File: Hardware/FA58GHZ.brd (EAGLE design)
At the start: 81.3 x 34.3 mm, 16 parts, among them U1 ATMEGA328P_TQFP, Y1 16MHZ

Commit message: Backup: Working in the Schematic, Footprints and PCB
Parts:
- added C10, C8, C9: 0.1uF, resistor:C0603
- added IC1: MAX4311EEE, maxim:QSOP16
- added JP3: (no value), SparkFun-Connectors:1X06
- added JP4: (no value), SparkFun-Connectors:1X04
- added R10, R11, R12: 1k, resistor:R0603
- added R5, R6, R7: 10k, resistor:R0603
- added R8: 470, resistor:R0603
- added R9: 5k1, resistor:R0603
- added SG1: BUZZERSMD, SparkFun-Electromechanical:BUZZER-CMT1603
- added U2: RX5808, FreakyAttic-EagleLibrary:RX5808
- added X1: SMA, con-coax:J502-ND-142-0701-881/886
- JP1: device SparkFun-Connectors:1X03 -> SparkFun-Connectors:1X03-1MM-RA
- R3, R4: value 10k -> ?
- moved U1 49.5 mm to (10.2, 58.4)
- moved JP1 3.17 mm to (20.3, 8.26)
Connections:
- net N$6 renamed LED
- new net BUT1: U1.32
- new net BUT2: U1.1
- new net CH1: R7.1, U1.14
- new net CH2: R5.1, U1.15
- new net CH3: R6.1, U1.16
- new net N$10: R12.1, U1.9
- new net N$11: SG1.P$2, U1.10
- new net N$12: R12.2, SG1.P$1
- new net N$13: R6.2, U2.P$9
- new net N$14: R5.2, U2.P$8
- new net N$15: R7.2, U2.P$7
- new net N$16: U2.P$11, X1.1
- new net N$6: R8.1, U1.11
- new net N$7: R9.1, U1.13
- new net N$8: R10.1, U1.30
- new net N$9: R11.1, U1.31
- new net OSD: IC1.5, R8.2, R9.2
- new net RSSI1: JP4.2, U1.19, U2.P$4
- new net RSSI2: JP4.4, U1.22
- new net SEL0: IC1.2
- new net SEL1: IC1.1
- new net VIDEO1: IC1.7, JP3.2, U2.P$2
- new net VIDEO2: IC1.10, JP3.4
- new net VIDEO3: IC1.12, JP3.6
- new net VIDEO_OUT: IC1.15, IC1.16
- net AN_VPOW: now also C9.2
- net GND: now also C10.1, C8.2, C9.1, IC1.13, JP3.1, JP3.3, JP3.5, JP4.1, JP4.3, U2.P$1, U2.P$10, U2.P$12, U2.P$6, X1.G@1, X1.G@2, X1.G@3, X1.G@4
- net VCC: now also C10.2, C8.1, IC1.14, IC1.4, U2.P$5
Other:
- board size 81.3 x 34.3 mm -> 108 x 78.7 mm

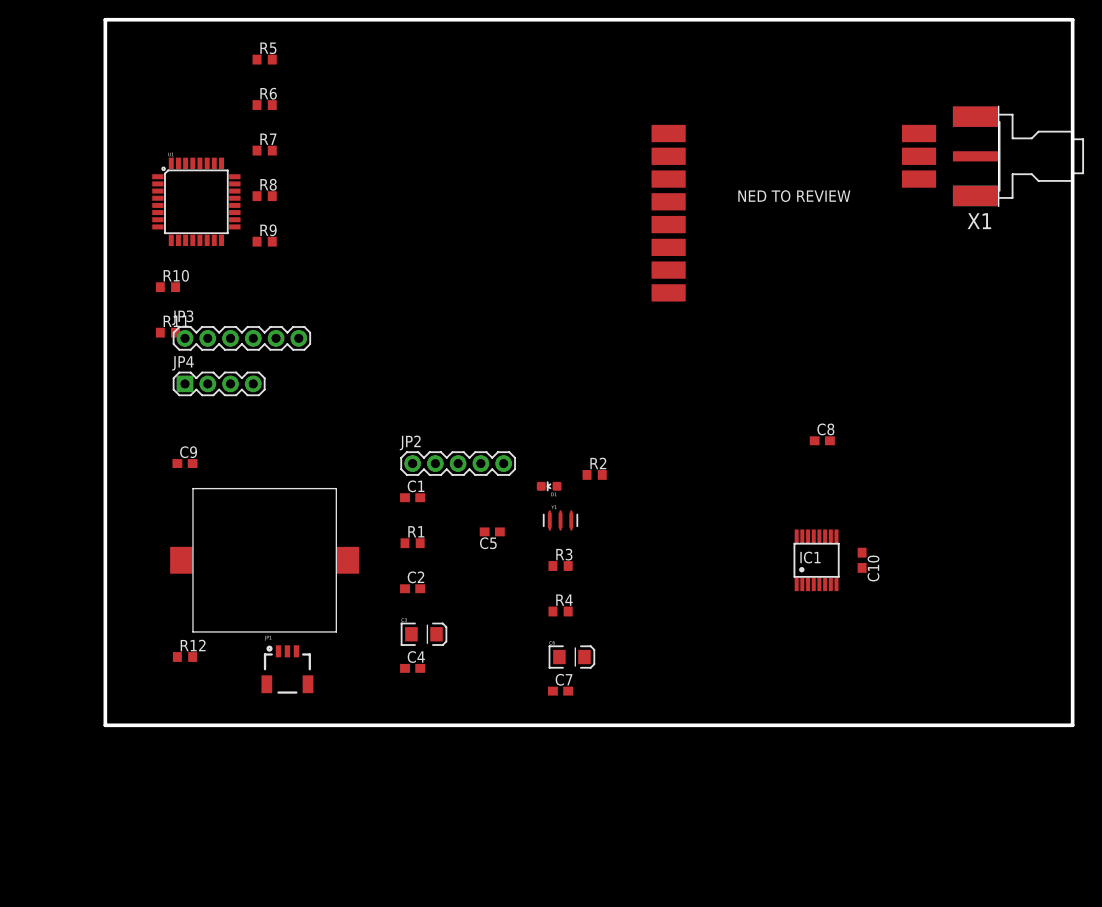
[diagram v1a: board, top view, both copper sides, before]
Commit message: Finish with the board Schematic, starting to code functions.
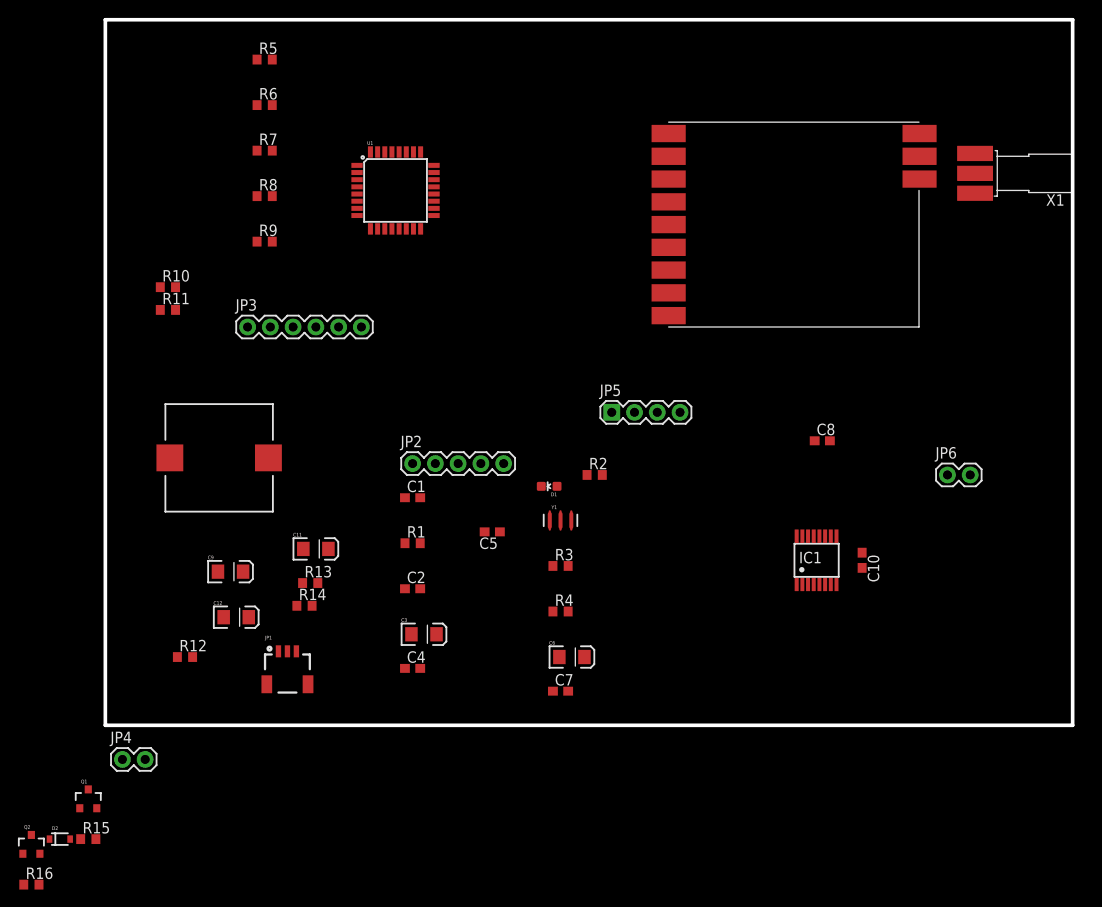
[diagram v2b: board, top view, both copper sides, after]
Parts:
- added C11, C12: 10uF, SparkFun-Capacitors:EIA3216
- added D2: Dio, SparkFun-DiscreteSemi:SOD-323
- added JP5: (no value), SparkFun-Connectors:1X04
- added JP6: (no value), SparkFun-Connectors:1X02
- added Q1, Q2: pchanel, SparkFun-DiscreteSemi:SOT23-3
- added R13, R14: 1k, resistor:R0603
- added R15, R16: 51k, resistor:R0603
- C9: value 0.1uF -> 10uF; device resistor:C0603 -> SparkFun-Capacitors:EIA3216
- JP4: value (none) -> FAN; device SparkFun-Connectors:1X04 -> FreakyAttic-EagleLibrary:1X02
- R5, R6, R7: value 10k -> 1k
- SG1: value BUZZERSMD -> BUZZERSMD3; device SparkFun-Electromechanical:BUZZER-CMT1603 -> FreakyAttic-EagleLibrary:BUZZER-12X12X3MM
- X1: value SMA -> SMA-SMDPCB; device con-coax:J502-ND-142-0701-881/886 -> FreakyAttic-EagleLibrary:SMA-PCB
- moved JP4 42.5 mm to (1.91, -3.81)
- moved U1 22.3 mm to (32.4, 59.7)
- moved C9 13.1 mm to (14.0, 17.1)
- moved SG1 12.5 mm to (12.7, 29.8)
- moved JP3 7.10 mm to (15.9, 44.5)
- moved X1 4.49 mm to (99.1, 59.1)
- moved R11 2.54 mm to (6.99, 46.4)
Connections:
- net N$13 renamed CLOCK
- net N$14 renamed SELECT
- net N$15 renamed DATA
- removed net RSSI2: JP4.4, U1.22
- new net BUT3: JP5.2
- new net FAN: Q1.1, R15.1
- new net N$17: C12.A, R14.1, U1.22
- new net N$18: C11.A, R13.1, U1.19
- new net N$19: D2.C, JP4.2, Q1.3
- new net N$20: C8.1, Q2.3, U2.P$5
- new net P-RF: Q2.1, R16.1
- net AN_VPOW: now also C9.A; no longer C9.2
- net BUT1: now also JP5.4
- net BUT2: now also JP5.3
- net GND: now also C11.C, C12.C, C9.C, D2.A, JP5.1, JP6.1, X1.P$1@1, X1.P$1@2; no longer C9.1, JP4.3, X1.G@1, X1.G@2, X1.G@3, X1.G@4
- net N$10: now also U1.25; no longer R12.1, U1.9
- net N$11: now also SG1.2, U1.26; no longer SG1.P$2, U1.10
- net N$12: now also SG1.1; no longer SG1.P$1
- net N$16: now also X1.P$2; no longer X1.1
- net RSSI1: no longer JP4.2, U1.19
- net VCC: now also Q1.2, Q2.2, R15.2, R16.2; no longer C8.1, U2.P$5
- net VIDEO_OUT: now also JP6.2

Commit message: Backup: Implemented OSD menu for Battery Monitor, needs to test it. - Modifications for the schematic - working on the PCB
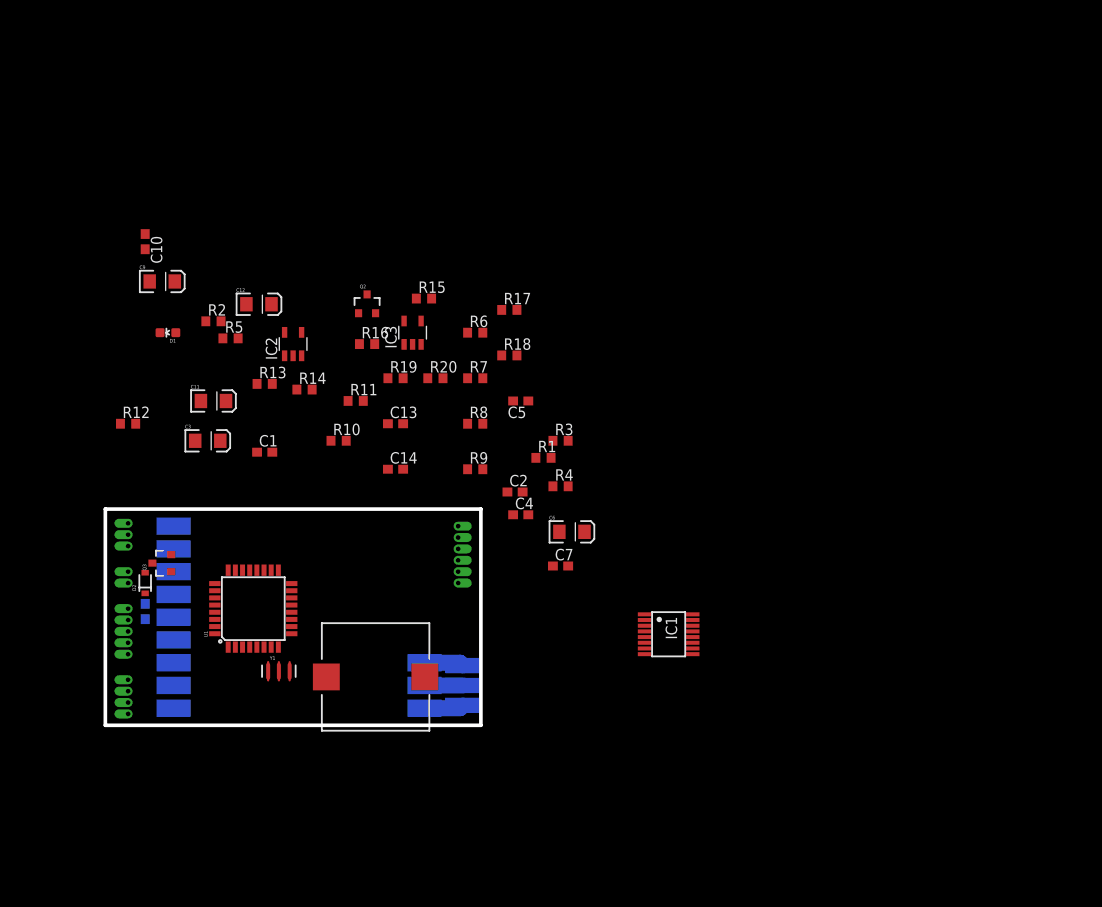
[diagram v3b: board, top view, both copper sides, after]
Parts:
- removed JP6: (no value), SparkFun-Connectors:1X02
- removed Q1: pchanel, SparkFun-DiscreteSemi:SOT23-3
- added C13, C14: 0.1uF, resistor:C0603
- added IC2, IC3: MCP6001, linear:SOT23-5
- added Q3: 200mA/50V, SparkFun-DiscreteSemi:SOT23-3
- added R17, R18, R19, R20: 51k, resistor:R0603
- D1: value (none) -> LED
- JP1: value PowerIn -> Power In; device SparkFun-Connectors:1X03-1MM-RA -> FreakyAttic-EagleLibrary:1X03-1.27MM-OFFSET
- JP2: value (none) -> Serial; device SparkFun-Connectors:1X05 -> FreakyAttic-EagleLibrary:1X05-1.27MM-OFFSET
- JP3: value (none) -> Video; device SparkFun-Connectors:1X06 -> FreakyAttic-EagleLibrary:1X06-1.27MM-OFFSET
- JP4: value FAN -> Fan; device FreakyAttic-EagleLibrary:1X02 -> FreakyAttic-EagleLibrary:1X02-1.27MM-OFFSET
- JP5: value (none) -> Button; device SparkFun-Connectors:1X04 -> FreakyAttic-EagleLibrary:1X04-1.27MM-OFFSET
- moved C10 87.6 mm to (4.45, 54.0)
- moved U2 84.6 mm to (7.62, 1.91), flipped to the bottom, turned to 180 degrees
- moved C8 77.9 mm to (4.45, 12.7), flipped to the bottom, turned to 90 degrees
- moved X1 77.3 mm to (41.9, 6.99), flipped to the bottom, turned to 0 degrees
- moved Q2 71.0 mm to (29.2, 47.0)
- moved R15 71.0 mm to (35.6, 47.6)
- moved R16 71.0 mm to (29.2, 42.5)
- moved JP5 61.7 mm to (2.54, 5.08), flipped to the bottom, turned to 270 degrees
- moved U1 49.3 mm to (16.5, 13.0), turned to 90 degrees
- moved D1 45.9 mm to (6.99, 43.8)
- moved R2 45.9 mm to (12.1, 45.1)
- moved JP3 37.0 mm to (39.4, 15.9), flipped to the bottom, turned to 90 degrees
- moved Y1 35.7 mm to (19.4, 6.03)
- moved JP2 35.6 mm to (2.54, 13.0), flipped to the bottom, turned to 270 degrees
- moved C12 35.0 mm to (17.1, 47.0)
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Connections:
- removed net N$19: D2.C, JP4.2, Q1.3
- new net +12V: C6.A, C7.2, D2.C, JP1.3, JP4.2, R3.2
- new net +5V: JP1.2
- new net AN_RSSI1: IC2.1, R13.2, R18.1
- new net AN_RSSI2: IC3.1, R14.2, R20.1
- new net N$13: D2.A, JP4.1, Q3.3
- new net N$14: IC2.4, R17.1, R18.2
- new net N$15: IC3.4, R19.1, R20.2
- new net RSSI2: IC3.3, JP3.4
- net AN_VPOW: now also U1.28
- net BUT3: now also U1.2
- net FAN: now also Q3.1, R15.2, U1.9; no longer Q1.1, R15.1
- net GND: now also C13.2, C14.2, IC2.2, IC3.2, JP3.6, Q3.2, R15.1, R17.2, R19.2; no longer D2.A, JP3.3, JP3.5, JP4.1, JP6.1
- net N$10: now also R12.1
- net P-RF: now also U1.10
- net RSSI1: now also IC2.3
- net RX: now also R10.2
- net SEL0: now also U1.23
- net SEL1: now also U1.24
- net TX: now also R11.2
- net VCC: now also C13.1, C14.1, IC2.5, IC3.5; no longer C6.A, C7.2, JP1.2, JP1.3, Q1.2, R15.2, R3.2
- net VIDEO1: no longer JP3.2
- net VIDEO2: now also JP3.3; no longer JP3.4
- net VIDEO3: now also JP3.2; no longer JP3.6
- net VIDEO_OUT: now also JP3.5; no longer JP6.2
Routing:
- net GND: track 0.00 -> 8.84 mm
- net N$16: track 0.00 -> 4.29 mm
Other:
- board size 108 x 78.7 mm -> 41.9 x 24.1 mm

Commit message: Backup: PCB routing finished, need to run DRC
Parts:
- C11, C12, C9: device SparkFun-Capacitors:EIA3216 -> SparkFun-Passives:0603-CAP
- Y1: device SparkFun-FreqCtrl:RESONATOR-SMD -> FreakyAttic-EagleLibrary:RESONATOR-SMD
- moved IC1 55.3 mm to (7.81, 4.51), turned to 90 degrees
- moved R17 50.6 mm to (21.3, 1.65), turned to 180 degrees
- moved C10 46.3 mm to (7.24, 7.75), turned to 0 degrees
- moved C12 45.4 mm to (30.0, 3.43), turned to 90 degrees
- moved Q2 43.8 mm to (5.08, 10.4), turned to 90 degrees
- moved C6 43.2 mm to (8.89, 21.3), turned to 270 degrees
- moved C2 41.5 mm to (4.45, 21.3), turned to 270 degrees
- moved R6 41.2 mm to (20.8, 8.00), turned to 270 degrees
- moved R18 41.0 mm to (24.5, 5.84), turned to 180 degrees
- moved C7 40.2 mm to (10.8, 21.9), turned to 270 degrees
- moved R7 40.1 mm to (18.2, 5.97), turned to 270 degrees
- moved D1 39.9 mm to (26.0, 8.76), turned to 270 degrees
- moved IC2 39.7 mm to (24.5, 3.05), turned to 180 degrees
- moved R3 39.4 mm to (12.9, 21.0), turned to 180 degrees
- moved IC3 39.4 mm to (32.9, 4.45), turned to 270 degrees
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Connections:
- removed net +5V: JP1.2
- net AN_VPOW: now also C9.1; no longer C9.A
- net BUT1: now also JP5.2; no longer JP5.4
- net BUT3: now also JP5.4; no longer JP5.2
- net GND: now also C11.2, C12.2, C9.2; no longer C11.C, C12.C, C9.C
- net N$17: now also C12.1; no longer C12.A
- net N$18: now also C11.1; no longer C11.A
- net RSSI2: now also JP3.5; no longer JP3.4
- net VCC: now also JP1.2
- net VIDEO2: now also JP3.2; no longer JP3.3
- net VIDEO3: now also JP3.3; no longer JP3.2
- net VIDEO_OUT: now also JP3.4; no longer JP3.5
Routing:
- net GND: track 8.84 -> 236.3 mm, vias 0 -> 4
- net VCC: track 0.00 -> 120.6 mm, vias 0 -> 10
- net +12V: track 0.00 -> 56.7 mm, vias 0 -> 2
- net RSSI2: track 0.00 -> 32.6 mm, vias 0 -> 2
- net SEL0: track 0.00 -> 29.4 mm, vias 0 -> 2
- net FAN: track 0.00 -> 29.1 mm, vias 0 -> 4
- net SEL1: track 0.00 -> 25.6 mm, vias 0 -> 2
- net CLOCK: track 0.00 -> 24.8 mm, vias 0 -> 1
- net N$11: track 0.00 -> 23.9 mm, vias 0 -> 2
- net SELECT: track 0.00 -> 21.6 mm, vias 0 -> 1
- net RSSI1: track 0.00 -> 21.0 mm, vias 0 -> 3
- net DTR: track 0.00 -> 20.9 mm, vias 0 -> 2
- net N$17: track 0.00 -> 19.8 mm
- net DATA: track 0.00 -> 18.9 mm, vias 0 -> 1
- net TX: track 0.00 -> 17.1 mm
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
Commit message: -Routing finished and DRC passed with approved warnings
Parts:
- moved Y1 0.13 mm to (10.8, 9.78)
- moved C10 0.13 mm to (7.37, 7.75)
- moved R10 0.13 mm to (24.3, 21.6)
- moved R8 0.06 mm to (14.5, 6.54)
- moved R9 0.06 mm to (14.5, 5.14)
- moved R5 0.06 mm to (19.5, 6.48)
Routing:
- net CLOCK: track 24.8 -> 23.9 mm
- net SEL1: track 25.6 -> 26.4 mm
- net RSSI1: track 21.0 -> 21.5 mm
- net RSSI2: track 32.6 -> 33.1 mm

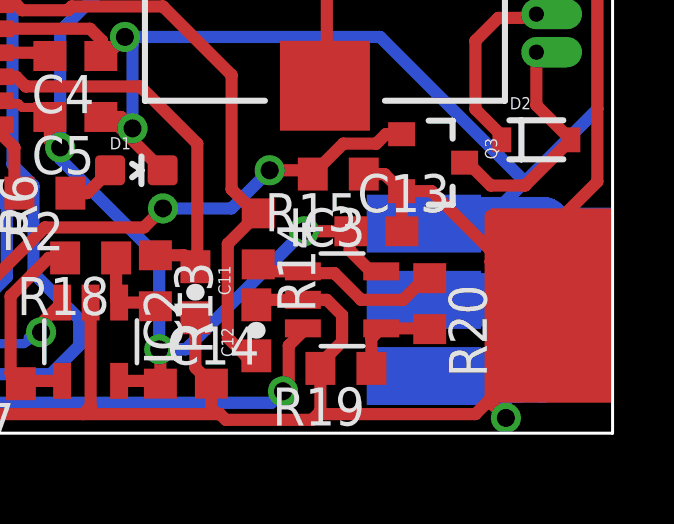
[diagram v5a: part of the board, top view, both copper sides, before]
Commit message: HARDWARE VERSION 1.0: CNC PCB prototype for testing.
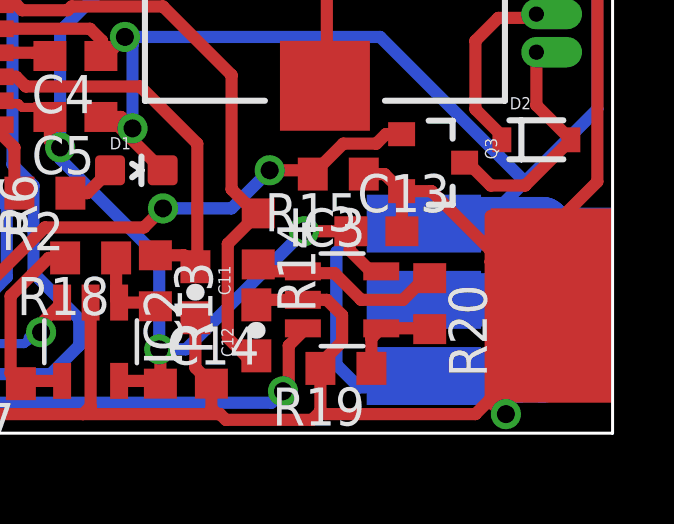
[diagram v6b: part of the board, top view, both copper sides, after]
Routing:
- net GND: track 236.6 -> 251.2 mm
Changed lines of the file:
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@@
 <layer number="21" name="tPlace" color="7" fill="1" visible="yes" active="yes"/>
 <layer number="22" name="bPlace" color="7" fill="1" visible="yes" active="yes"/>
-<layer number="23" name="tOrigins" color="15" fill="1" visible="no" active="yes"/>
-<layer number="24" name="bOrigins" color="15" fill="1" visible="no" active="yes"/>
+<layer number="23" name="tOrigins" color="15" fill="1" visible="yes" active="yes"/>
+<layer number="24" name="bOrigins" color="15" fill="1" visible="yes" active="yes"/>
 <layer number="25" name="tNames" color="7" fill="1" visible="no" active="yes"/>
 <layer number="26" name="bNames" color="7" fill="1" visible="no" active="yes"/>
@@
 <wire x1="39.5925" y1="1.905" x2="39.91" y2="2.2225" width="1.778" layer="16"/>
 <wire x1="35.62" y1="6.985" x2="37.592" y2="6.985" width="1.778" layer="16"/>
-<wire x1="37.592" y1="6.985" x2="39.5925" y2="6.985" width="1.778" layer="16"/>
+<wire x1="37.592" y1="6.985" x2="38.2905" y2="6.985" width="1.778" layer="16"/>
+<wire x1="38.2905" y1="6.985" x2="39.5925" y2="6.985" width="1.778" layer="16"/>
 <wire x1="39.5925" y1="6.985" x2="39.91" y2="6.6675" width="1.778" layer="16"/>
 <contactref element="Y1" pad="2"/>
@@
 <wire x1="20.486" y1="0.674" x2="20.447" y2="0.635" width="0.4064" layer="1"/>
 <wire x1="37.846" y1="1.143" x2="37.846" y2="1.016" width="0.4064" layer="1"/>
-<wire x1="37.846" y1="1.016" x2="38.354" y2="0.508" width="0.4064" layer="1"/>
-<via x="38.354" y="0.508" extent="1-16" drill="0.6" shape="octagon"/>
-<wire x1="38.354" y1="0.508" x2="38.354" y2="1.524" width="0.4064" layer="16"/>
+<wire x1="37.846" y1="1.016" x2="38.354" y2="0.635" width="0.4064" layer="1"/>
+<via x="38.354" y="0.635" extent="1-16" drill="0.6" shape="octagon"/>
 <wire x1="38.354" y1="1.524" x2="38.735" y2="1.905" width="0.4064" layer="16"/>
 <wire x1="24.853" y1="10.541" x2="25.134" y2="10.541" width="0.4064" layer="1"/>
@@
 <wire x1="29.0195" y1="0.4445" x2="31.8915" y2="0.4445" width="0.4064" layer="1"/>
 <wire x1="31.8915" y1="0.4445" x2="32.17" y2="0.723" width="0.4064" layer="1"/>
+<wire x1="38.354" y1="1.524" x2="33.4645" y2="1.524" width="0.4064" layer="16"/>
+<wire x1="33.4645" y1="1.524" x2="32.7025" y2="2.286" width="0.4064" layer="16"/>
+<wire x1="32.7025" y1="2.286" x2="32.7025" y2="6.0325" width="0.4064" layer="16"/>
+<wire x1="32.7025" y1="6.0325" x2="33.401" y2="6.731" width="0.4064" layer="16"/>
+<wire x1="33.401" y1="6.731" x2="38.0365" y2="6.731" width="0.4064" layer="16"/>
+<wire x1="38.0365" y1="6.731" x2="38.2905" y2="6.985" width="0.4064" layer="16"/>
 </signal>
 <signal name="N$1">
